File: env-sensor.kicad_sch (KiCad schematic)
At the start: 7 parts, among them U1401 BME280

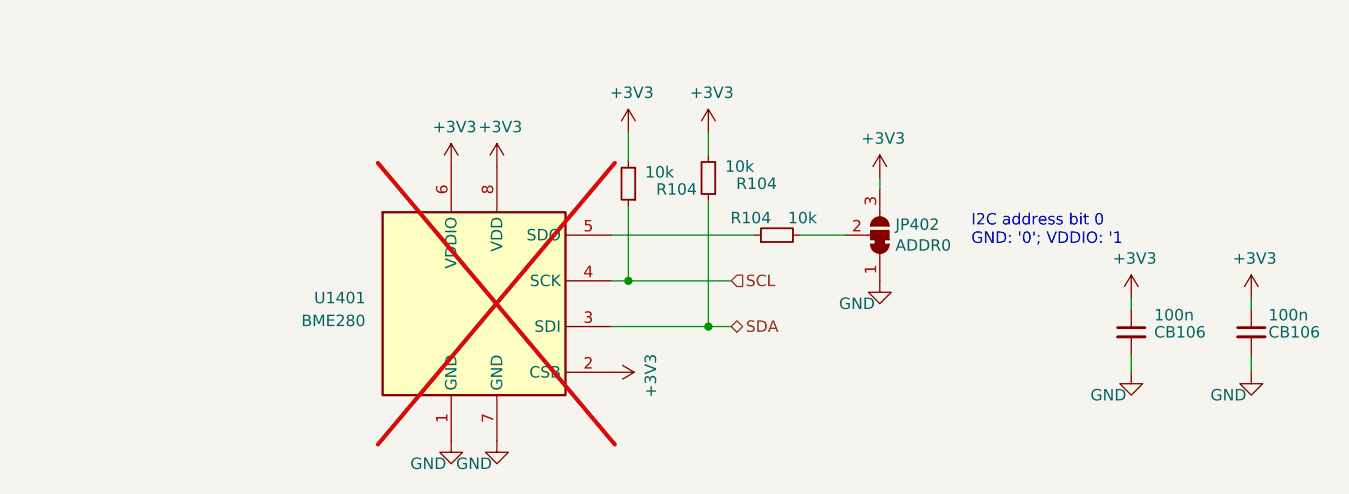
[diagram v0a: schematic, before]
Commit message: (sch) change to 100k pull-ups
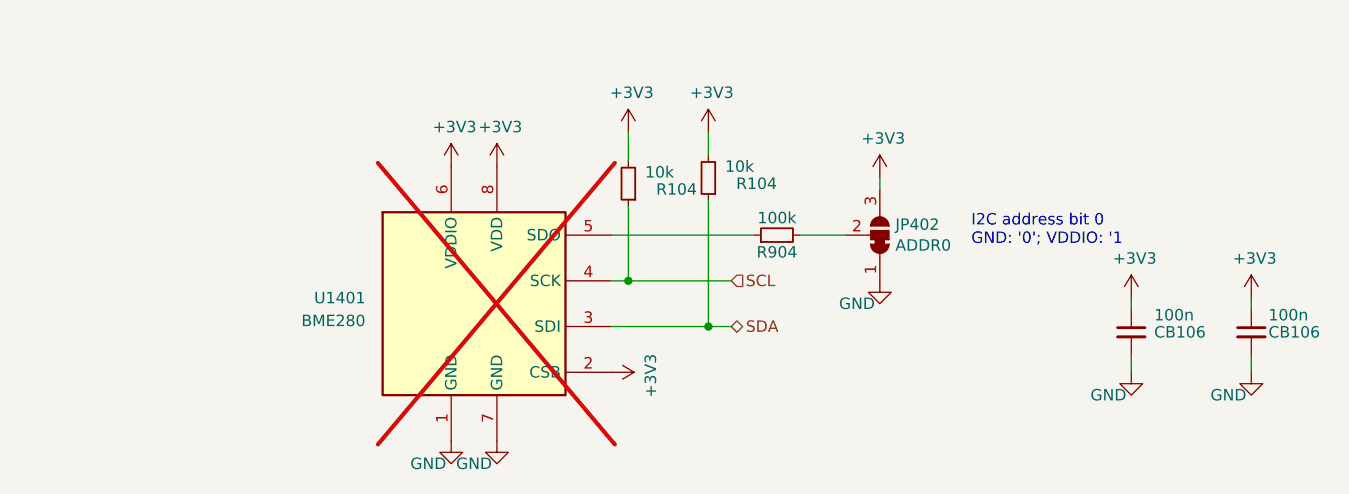
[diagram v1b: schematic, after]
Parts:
- removed R104: 10k, Resistor_SMD:R_0402_1005Metric, symbol Device:R_Small
- added R904: 100k, Resistor_SMD:R_0402_1005Metric, symbol Device:R_Small
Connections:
- net at U1401.5 (SDO): now also R904.1
- net at JP402.2 (C): now also R904.2
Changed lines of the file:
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@@
+    )
+  )
+  (symbol (lib_id "Device:R_Small") (at 118.11 83.185 90) (unit 1)
+    (in_bom yes) (on_board yes) (dnp no)
+    (property "Reference" "R904" (at 118.11 85.09 90)
+      (effects (font (size 1.27 1.27)))
+    )
+    (property "Value" "100k" (at 118.11 81.28 90)
+      (effects (font (size 1.27 1.27)))
+    )
+    (property "Footprint" "Resistor_SMD:R_0402_1005Metric" (at 118.11 83.185 0)
+      (effects (font (size 1.27 1.27)) hide)
+    )
+    (property "Datasheet" "~" (at 118.11 83.185 0)
+      (effects (font (size 1.27 1.27)) hide)
+    )
+    (property "MPN" "RT0402FRE07100KL" (at 118.11 83.185 0)
+      (effects (font (size 1.27 1.27)) hide)
+    )
+    (property "Mfr." "Yageo" (at 118.11 83.185 0)
+      (effects (font (size 1.27 1.27)) hide)
+    )
+    (pin "1")
+    (pin "2")
+    (instances
+      (project "kleinvoet"
+        (path "/4185c36c-c66e-4dbd-be5d-841e551f4885/00000000-0000-0000-0000-00005eede770"
+          (reference "R904") (unit 1)
+        )
+        (path "/4185c36c-c66e-4dbd-be5d-841e551f4885/6761cd4a-72b1-4e84-88a1-1fb4245924b8"
+          (reference "R1403") (unit 1)
+        )
+      )
     )
   )
@@
         )
       )
-    )
-  )
-  (symbol (lib_id "Device:R_Small") (at 118.11 83.185 90) (unit 1)
-    (in_bom yes) (on_board yes) (dnp no)
-    (property "Reference" "R104" (at 117.475 81.28 90)
-      (effects (font (size 1.27 1.27)) (justify left))
-    )
-    (property "Value" "10k" (at 122.555 81.28 90)
-      (effects (font (size 1.27 1.27)) (justify left))
-    )
-    (property "Footprint" "Resistor_SMD:R_0402_1005Metric" (at 118.11 83.185 0)
-      (effects (font (size 1.27 1.27)) hide)
-    )
-    (property "Datasheet" "~" (at 118.11 83.185 0)
-      (effects (font (size 1.27 1.27)) hide)
-    )
-    (property "MPN" "RT0402FRE1310KL" (at 118.11 83.185 0)
-      (effects (font (size 1.27 1.27)) hide)
-    )
-    (property "Mfr." "Yageo" (at 118.11 83.185 0)
-      (effects (font (size 1.27 1.27)) hide)
-    )
-    (pin "1")
-    (pin "2")
-    (instances
-      (project "kleinvoet"
-        (path "/4185c36c-c66e-4dbd-be5d-841e551f4885"
-          (reference "R104") (unit 1)
-        )
-        (path "/4185c36c-c66e-4dbd-be5d-841e551f4885/6761cd4a-72b1-4e84-88a1-1fb4245924b8"
-          (reference "R1403") (unit 1)
-        )
-      )

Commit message: (sch) remove pull-up R I2C for BME280
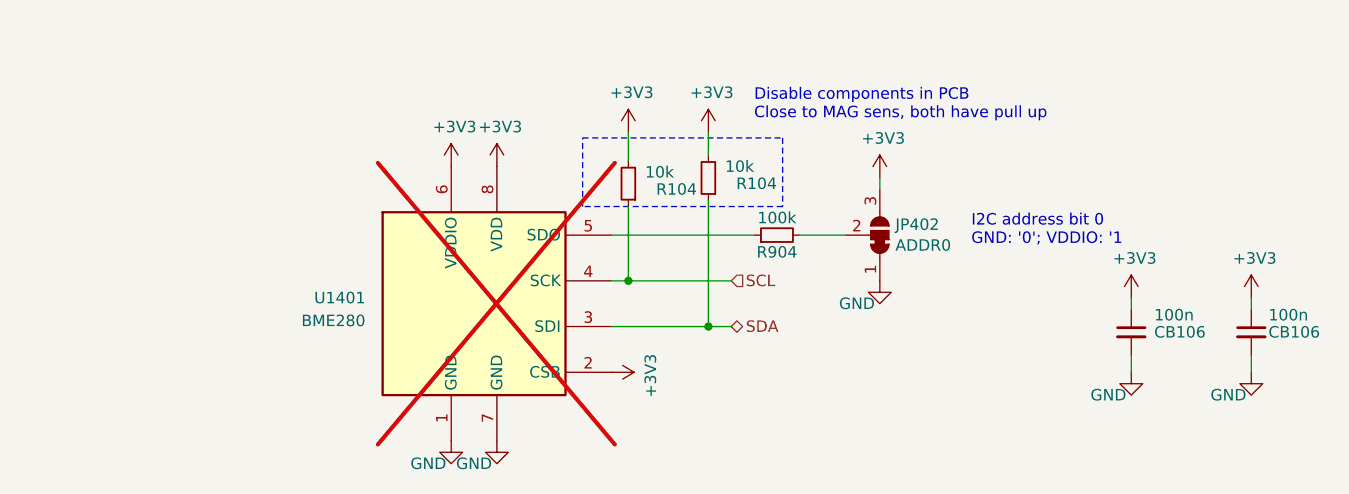
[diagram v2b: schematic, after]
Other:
- note added: "Disable components in PCB Close to MAG sens, both have pull up"
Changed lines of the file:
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@@
     (stroke (width 0) (type default))
+  )
+  (rectangle (start 96.52 72.39) (end 118.745 80.01)
+    (stroke (width 0) (type dash))
+    (fill (type none))
+  )
+  (text "Disable components in PCB\nClose to MAG sens, both have pull up"
+    (at 115.57 70.485 0)
+    (effects (font (size 1.27 1.27)) (justify left bottom))
   )
   (text "I2C address bit 0\nGND: '0'; VDDIO: '1" (at 139.7 84.455 0)
@@
         )
         (path "/4185c36c-c66e-4dbd-be5d-841e551f4885/6761cd4a-72b1-4e84-88a1-1fb4245924b8"
-          (reference "R1402") (unit 1)
+          (reference "#R1402") (unit 1)
         )
       )
@@
         )
         (path "/4185c36c-c66e-4dbd-be5d-841e551f4885/6761cd4a-72b1-4e84-88a1-1fb4245924b8"
-          (reference "R1401") (unit 1)
-        )
-      )
+          (reference "#R1401") (unit 1)
+        )
+      )

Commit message: (sch) annotate env-sens pins
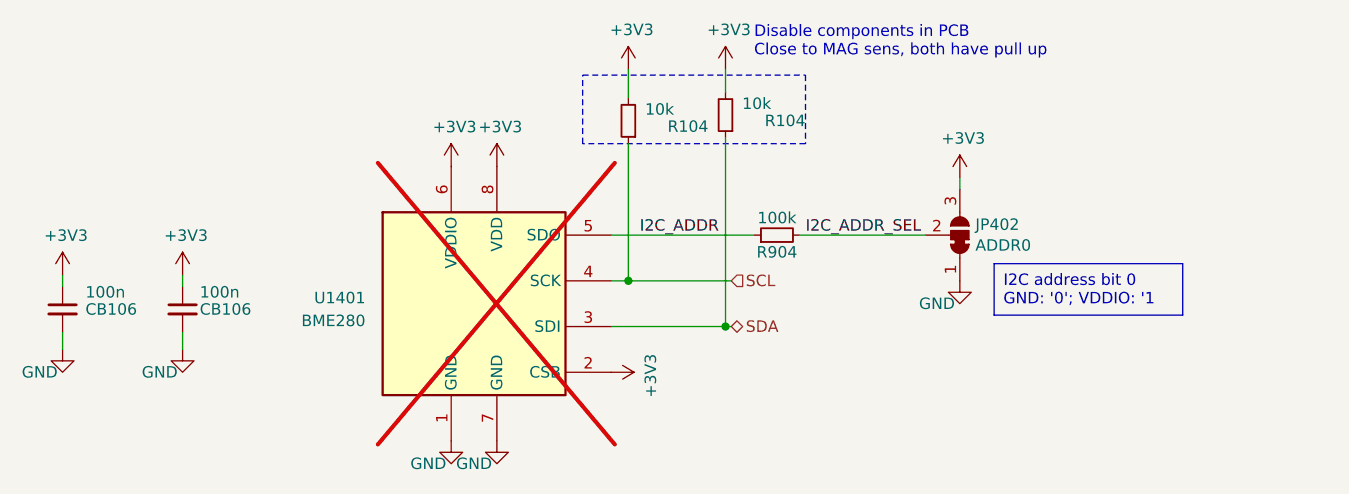
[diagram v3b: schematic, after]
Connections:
- net I2C_ADDR: now reaches R904.1, U1401.5 (SDO)
- net I2C_ADDR_SEL: now reaches JP402.2 (C), R904.2
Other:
- note removed: "I2C address bit 0 GND: '0'; VDDIO: '1"
- moved on the sheet: CB106, JP402, R104

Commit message: (sch) update title block
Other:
- company: (none) -> Department of Electrical and Electronic Engineering - Stellenbosch University
- title: (none) -> Kleinvoet
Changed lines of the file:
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@@
 (kicad_sch (version 20230121) (generator eeschema)
   (paper "A4")
+  (title_block
+    (title "Kleinvoet")
+    (date "2023-04-12")
+    (rev "C")
+    (company "Department of Electrical and Electronic Engineering - Stellenbosch University")
+    (comment 1 "Digital Signal Processing Laboratory")
+    (comment 2 "Author: CM Geldenhuys <cmgeldenhuys@sun.ac.za>")
+    (comment 3 "Project: Kleinvoet")
+    (comment 4 "License: CERN-OHL-S-2.0")
+  )
   (junction (at 101.6 88.265) (diameter 0) (color 0 0 0 0)
   )
